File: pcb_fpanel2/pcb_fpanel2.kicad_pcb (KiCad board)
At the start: 2 copper layers, 11 parts, among them J1 Conn_01x09, SW1 SW_Push_LED, SW2 SW_Push_LED, SW3 SW_Push_LED, SW4 SW_Push_LED, SW5 SW_Push_LED

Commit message: Frontpanel pcb valmis
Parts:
- added D6: D, Diodes_THT:D_DO-35_SOD27_P7.62mm_Horizontal, F.Cu at (182.0, 117.0)
- added D7: D, Diodes_THT:D_DO-35_SOD27_P7.62mm_Horizontal, F.Cu at (178.0, 117.0)
- added D8: D, Diodes_THT:D_DO-35_SOD27_P7.62mm_Horizontal, F.Cu at (174.0, 117.0)
- added D9: D, Diodes_THT:D_DO-35_SOD27_P7.62mm_Horizontal, F.Cu at (170.0, 117.0)
- added REF**: MountingHole_4.3mm_M4, Mounting_Holes:MountingHole_4.3mm_M4, F.Cu at (140.0, 155.0)
- added REF**: MountingHole_4.3mm_M4, Mounting_Holes:MountingHole_4.3mm_M4, F.Cu at (60.0, 135.0)
- added REF**: MountingHole_4.3mm_M4, Mounting_Holes:MountingHole_4.3mm_M4, F.Cu at (140.0, 110.0)
- added SW6: SW_Push_LED, MX_Alps_Hybrid:MX-1U, F.Cu at (155.4, 138.4)
- added SW7: SW_Push_LED, MX_Alps_Hybrid:MX-1U, F.Cu at (155.4, 157.5)
- added SW8: SW_Push_LED, MX_Alps_Hybrid:MX-1U, F.Cu at (174.5, 157.5)
- added SW9: SW_Push_LED, MX_Alps_Hybrid:MX-1U, F.Cu at (174.4, 138.4)
- J1: value Conn_01x09 -> Conn_01x10; footprint Pin_Headers:Pin_Header_Straight_1x09_Pitch2.54mm -> Pin_Headers:Pin_Header_Straight_1x10_Pitch2.54mm; moved to B.Cu
- moved J1 116.4 mm to (142.0, 146.0)
- moved D3 84.6 mm to (129.0, 116.2)
- moved D4 84.6 mm to (129.0, 120.0)
- moved D5 84.6 mm to (129.0, 123.8)
- moved D2 83.7 mm to (113.0, 127.0)
- moved D1 81.4 mm to (113.0, 131.0)
- moved SW5 81.0 mm to (63.4, 112.0)
- moved SW3 80.9 mm to (101.5, 112.0)
- moved SW4 80.9 mm to (82.5, 112.0)
- moved SW1 69.2 mm to (126.3, 138.4)
- moved SW2 68.9 mm to (38.5, 138.4)
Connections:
- net Net-(D1-Pad1) renamed row_1
- J1 pad 1: Net-(J1-Pad1) -> led_1
- J1 pad 2: Net-(J1-Pad2) -> led_2
- J1 pad 3: Net-(J1-Pad3) -> GNDD
- J1 pad 4: Net-(J1-Pad4) -> column_1
- J1 pad 5: Net-(J1-Pad5) -> column_2
- J1 pad 7: Net-(J1-Pad7) -> column_3
- J1 pad 8: Net-(J1-Pad8) -> column_4
- J1 pad 9: Net-(J1-Pad9) -> column_5
- SW1 pad 2: Net-(J1-Pad5) -> column_1
- SW1 pad 3: Net-(J1-Pad7) -> led_2
- SW1 pad 4: Net-(J1-Pad8) -> GNDD
- SW2 pad 2: Net-(J1-Pad4) -> column_2
- SW2 pad 3: Net-(J1-Pad9) -> led_1
- SW2 pad 4: Net-(J1-Pad8) -> GNDD
- SW3 pad 2: Net-(J1-Pad3) -> column_3
- SW4 pad 2: Net-(J1-Pad2) -> column_4
- SW5 pad 2: Net-(J1-Pad1) -> column_5
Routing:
- net column_2: track 0.00 -> 158.4 mm
- net Net-(J1-Pad4): track 154.2 -> 0.00 mm
- net Net-(J1-Pad9): track 145.2 -> 0.00 mm
- net Net-(J1-Pad8): track 144.5 -> 0.00 mm
- net led_1: track 0.00 -> 119.7 mm
- net Net-(J1-Pad1): track 116.1 -> 0.00 mm
- net column_4: track 0.00 -> 112.8 mm
- net Net-(D6-Pad2): track 0.00 -> 104.4 mm
- net column_3: track 0.00 -> 104.1 mm
- net Net-(J1-Pad2): track 95.3 -> 0.00 mm
- net column_5: track 0.00 -> 92.1 mm
- net Net-(D7-Pad2): track 0.00 -> 85.0 mm
- net Net-(J1-Pad5): track 76.2 -> 0.00 mm
- net Net-(J1-Pad3): track 75.5 -> 0.00 mm
- net Net-(J1-Pad7): track 62.1 -> 0.00 mm
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- added copper zone on B.Cu, net GNDD
- removed copper zone on F.Cu, net (none)
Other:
- board outline added: 155 x 65 mm
- net class Default: clearance 0.2 -> 0.4; trace_width 0.25 -> 0.4
- rule trace_clearance: 0.2 -> 0.4

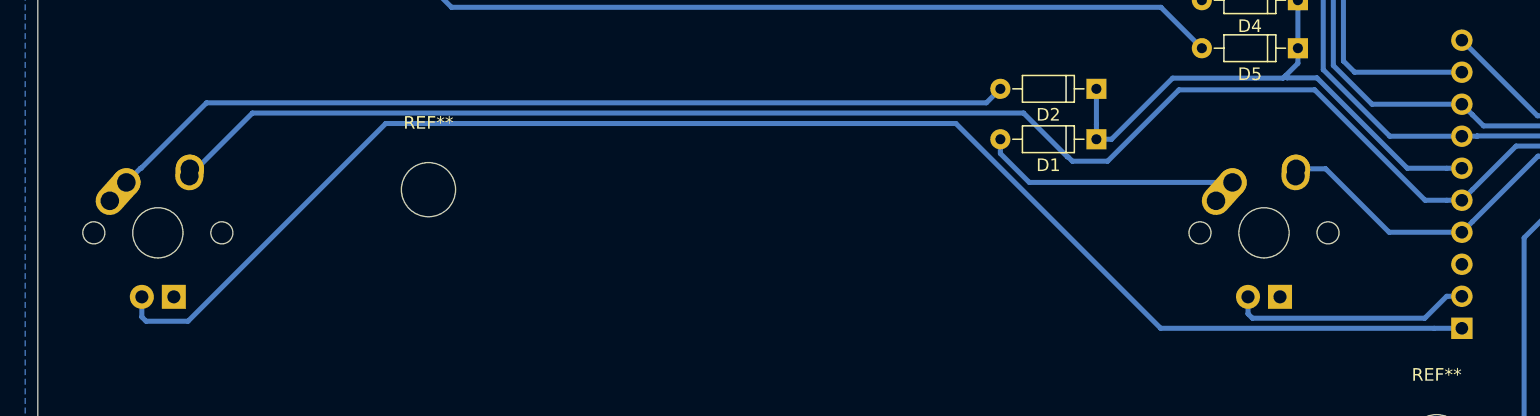
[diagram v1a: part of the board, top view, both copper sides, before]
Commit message: Frontpanel pcb korjaus: led-napit käännetty ja yhteensopivuus arduino pro micron kanssa
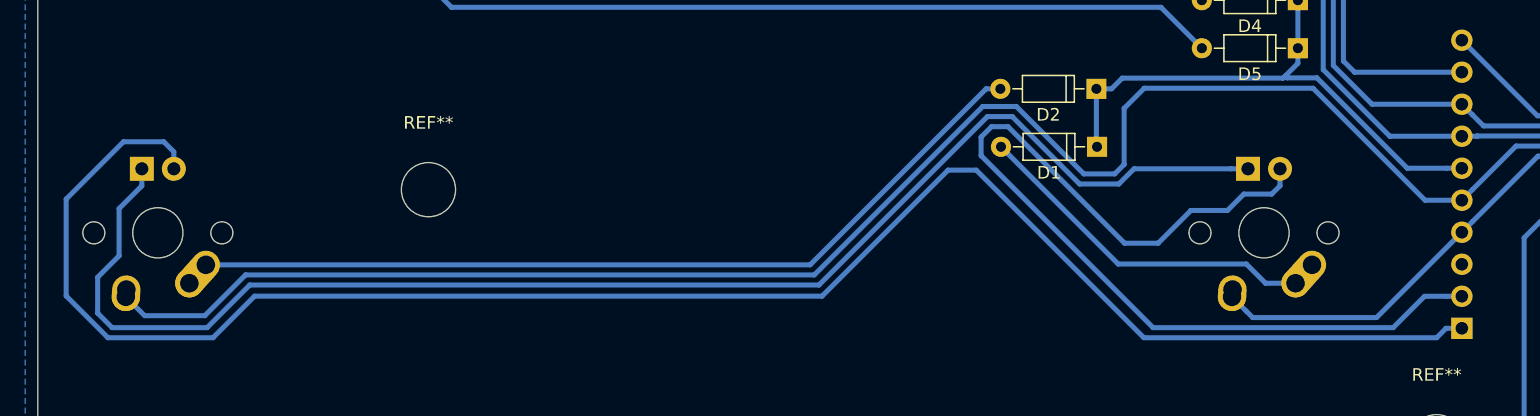
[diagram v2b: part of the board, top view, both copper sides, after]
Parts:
- moved D1 0.60 mm to (113.0, 131.6)
- turned SW1 to 180 degrees
- turned SW2 to 180 degrees
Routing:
- net GNDD: track 0.00 -> 114.3 mm
- net led_2: track 19.2 -> 77.4 mm
- net led_1: track 119.7 -> 143.2 mm
- net column_2: track 158.4 -> 172.6 mm
- net Net-(D1-Pad2): track 20.5 -> 27.9 mm
- net column_1: track 34.3 -> 40.8 mm
- net Net-(D2-Pad2): track 72.4 -> 68.8 mm
- net row_1: track 48.3 -> 47.3 mm

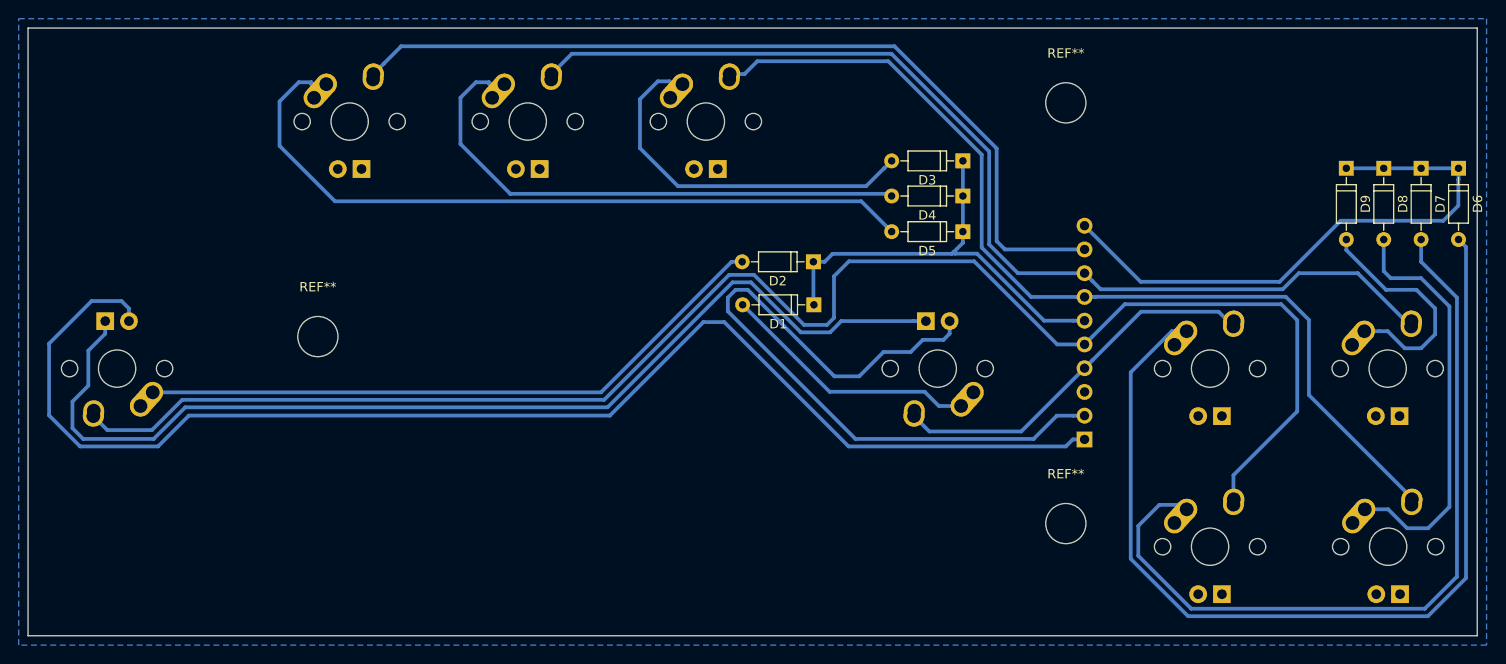
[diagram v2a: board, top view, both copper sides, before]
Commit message: fpanel1 ja fpanel2 välisen liittimen pin-järjestys korjattu vastaamaan toisiaan
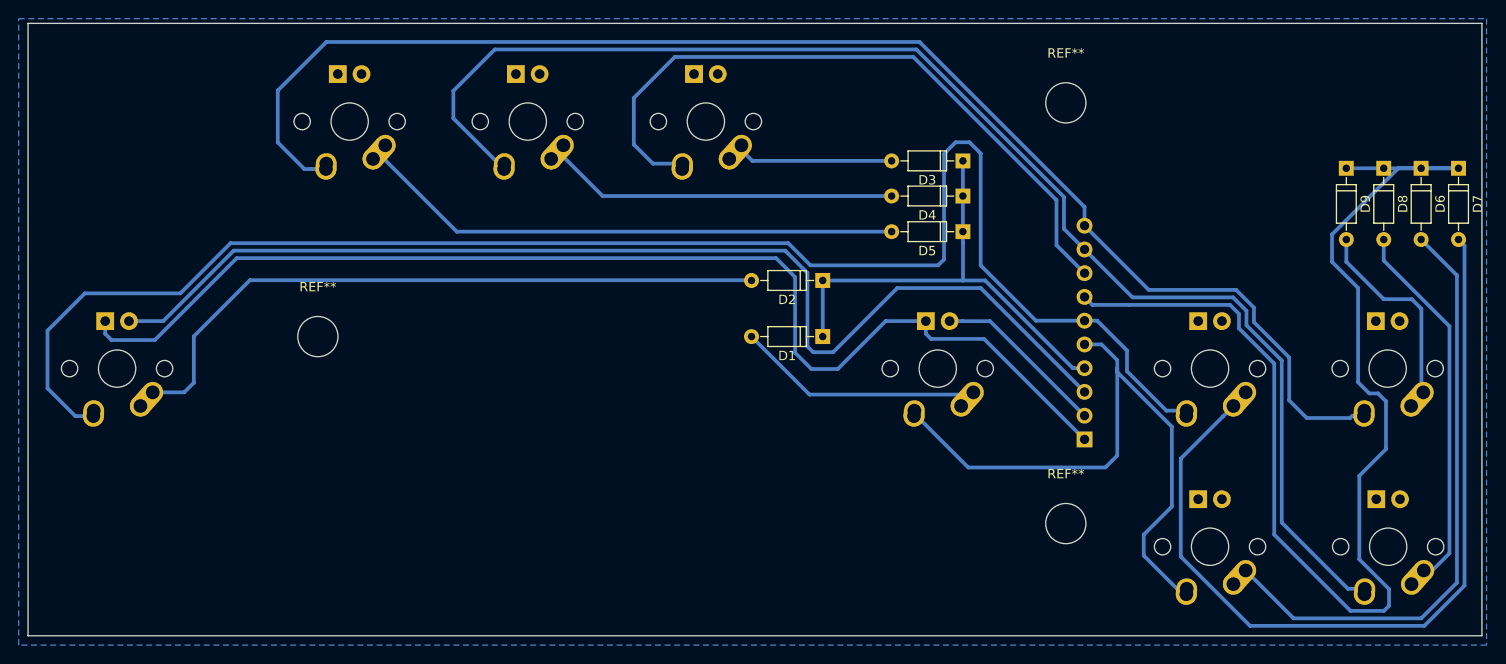
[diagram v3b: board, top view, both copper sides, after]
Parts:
- moved SW6 19.0 mm to (155.4, 157.5), turned to 180 degrees
- moved SW7 19.0 mm to (155.4, 138.4), turned to 180 degrees
- moved D6 4.00 mm to (178.0, 117.0)
- moved D7 4.00 mm to (182.0, 117.0)
- moved D1 3.53 mm to (114.0, 135.0)
- moved D2 2.24 mm to (114.0, 129.0)
- turned SW3 to 180 degrees
- turned SW4 to 180 degrees
- turned SW5 to 180 degrees
- turned SW8 to 180 degrees
- turned SW9 to 180 degrees
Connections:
- J1 pad 1: led_1 -> GNDD
- J1 pad 10: row_2 -> column_4
- J1 pad 3: GNDD -> led_1
- J1 pad 4: column_1 -> row_1
- J1 pad 5: column_2 -> column_1
- J1 pad 6: row_1 -> column_2
- J1 pad 7: column_3 -> row_2
- J1 pad 8: column_4 -> column_5
- J1 pad 9: column_5 -> column_3
- SW3 pad 2: column_3 -> column_5
- SW4 pad 2: column_4 -> column_3
- SW5 pad 2: column_5 -> column_4
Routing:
- net row_2: track 61.8 -> 131.9 mm
- net led_2: track 77.4 -> 18.6 mm
- net column_3: track 104.1 -> 146.9 mm
- net Net-(D6-Pad2): track 104.4 -> 64.6 mm
- net column_4: track 112.8 -> 151.7 mm
- net column_1: track 40.8 -> 69.1 mm
- net Net-(D3-Pad2): track 40.4 -> 17.0 mm
- net led_1: track 143.2 -> 121.9 mm
- net Net-(D5-Pad2): track 80.1 -> 58.9 mm
- net Net-(D4-Pad2): track 58.9 -> 38.1 mm
- net column_5: track 92.1 -> 73.5 mm
- net GNDD: track 114.3 -> 127.8 mm
- net Net-(D7-Pad2): track 85.0 -> 90.9 mm
- net Net-(D8-Pad2): track 44.3 -> 40.0 mm
- net row_1: track 47.3 -> 50.7 mm
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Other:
- board size 155 x 65 mm -> 155.5 x 65.5 mm

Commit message: Näppäinmatriisin srakkeille lisätty etuvastukset
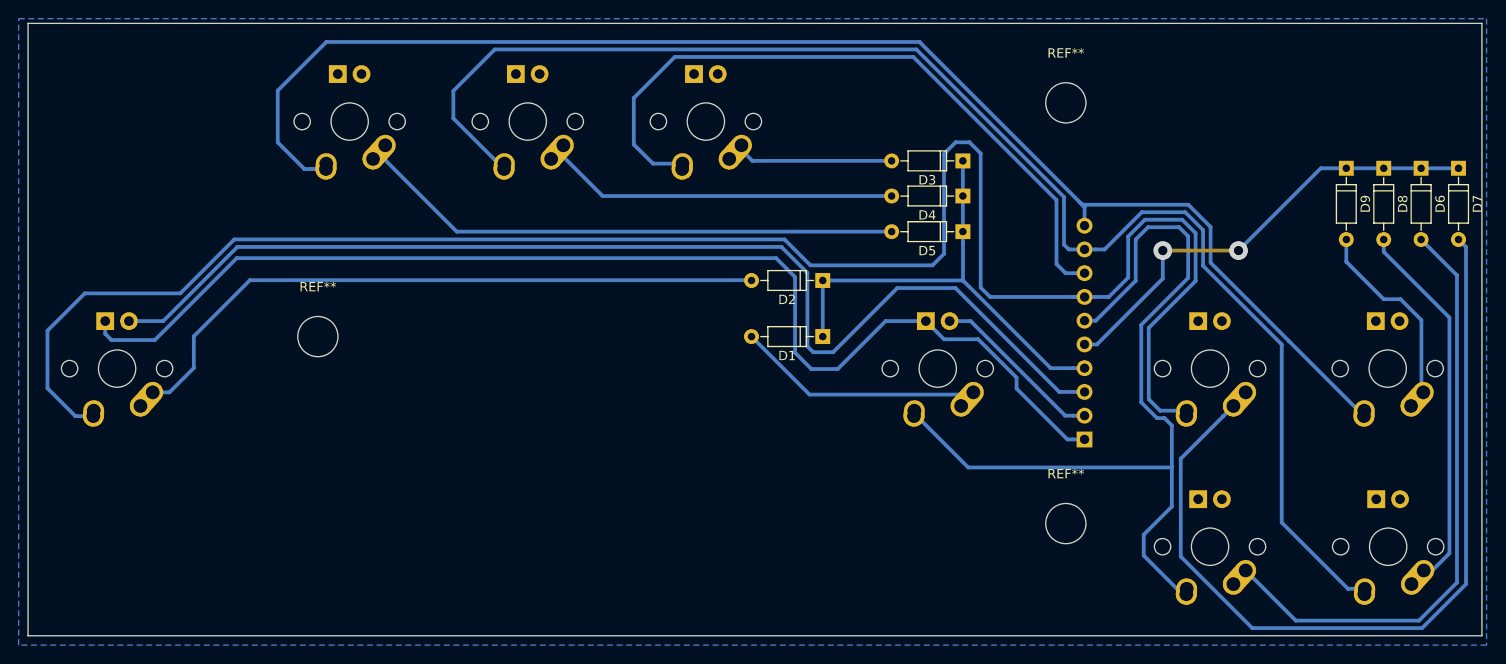
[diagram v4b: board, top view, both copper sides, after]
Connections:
- J1 pad 5: column_1 -> row_2
- J1 pad 6: column_2 -> column_1
- J1 pad 7: row_2 -> column_2
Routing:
- net row_2: track 131.9 -> 49.6 mm, vias 0 -> 2
- net column_2: track 171.6 -> 198.5 mm
- net column_1: track 69.1 -> 93.8 mm
- net column_3: track 146.9 -> 153.5 mm
- net column_5: track 73.5 -> 74.6 mm
- net Net-(D2-Pad2): track 71.9 -> 71.0 mm
- net Net-(D9-Pad2): track 21.5 -> 20.8 mm
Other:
- net class Default: via_dia 0.8 -> 2; via_drill 0.4 -> 1

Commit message: Reikien siirtelyä
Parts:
- moved REF** 33.8 mm to (108.0, 144.0)
- moved REF** 30.5 mm to (34.0, 119.0)
- moved REF** 19.4 mm to (159.4, 109.0)
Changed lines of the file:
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@@
   (general
     (thickness 1.6)
-    (drawings 6)
+    (drawings 10)
     (tracks 193)
     (zones 0)
@@
     (visible_elements 7FFFFFFF)
     (pcbplotparams
-      (layerselection 0x010fc_ffffffff)
+      (layerselection 0x00000_fffffffe)
       (usegerberextensions false)
       (usegerberattributes false)
@@
       (excludeedgelayer true)
       (linewidth 0.100000)
-      (plotframeref false)
+      (plotframeref true)
       (viasonmask false)
       (mode 1)
@@
       (psnegative false)
       (psa4output false)
-      (plotreference true)
-      (plotvalue true)
+      (plotreference false)
+      (plotvalue false)
       (plotinvisibletext false)
-      (padsonsilk false)
+      (padsonsilk true)
       (subtractmaskfromsilk false)
-      (outputformat 1)
+      (outputformat 5)
       (mirror false)
       (drillshape 1)
       (scaleselection 1)
-      (outputdirectory ""))
+      (outputdirectory "./"))
   )
   (net 0 "")
@@
   )
   (module Mounting_Holes:MountingHole_4.3mm_M4 (layer F.Cu)
-    (at 140 155)
+    (at 108 144)
     (descr "Mounting Hole 4.3mm, no annular, M4")
     (tags "mounting hole 4.3mm no annular m4")
@@
   )
   (module Mounting_Holes:MountingHole_4.3mm_M4 (layer F.Cu)
-    (at 60 135)
+    (at 34 119)
     (descr "Mounting Hole 4.3mm, no annular, M4")
     (tags "mounting hole 4.3mm no annular m4")
@@
   )
   (module Mounting_Holes:MountingHole_4.3mm_M4 (layer F.Cu)
-    (at 140 110)
+    (at 159.4 109)
     (descr "Mounting Hole 4.3mm, no annular, M4")
     (tags "mounting hole 4.3mm no annular m4")
@@
       (net 23 column_4))
   )
+  (dimension 19.9 (width 0.12) (layer F.SilkS)
+    (gr_text "19.900 mm" (at 160.67 118.95 90) (layer F.SilkS)
+      (effects (font (size 1 1) (thickness 0.15)))
+    )
+    (feature1 (pts (xy 159.4 109) (xy 159.986421 109)))
+    (feature2 (pts (xy 159.4 128.9) (xy 159.986421 128.9)))
+    (crossbar (pts (xy 159.4 128.9) (xy 159.4 109)))
+    (arrow1a (pts (xy 159.4 109) (xy 159.986421 110.126504)))
+    (arrow1b (pts (xy 159.4 109) (xy 158.813579 110.126504)))
+    (arrow2a (pts (xy 159.4 128.9) (xy 159.986421 127.773496)))
+    (arrow2b (pts (xy 159.4 128.9) (xy 158.813579 127.773496)))
+  )
+  (dimension 13.5 (width 0.12) (layer F.SilkS)
+    (gr_text "13.500 mm" (at 152.65 108.13) (layer F.SilkS)
+      (effects (font (size 1 1) (thickness 0.15)))
+    )
+    (feature1 (pts (xy 159.4 128.9) (xy 159.4 108.813579)))
+    (feature2 (pts (xy 145.9 128.9) (xy 145.9 108.813579)))
+    (crossbar (pts (xy 145.9 109.4) (xy 159.4 109.4)))
+    (arrow1a (pts (xy 159.4 109.4) (xy 158.273496 109.986421)))
+    (arrow1b (pts (xy 159.4 109.4) (xy 158.273496 108.813579)))
+    (arrow2a (pts (xy 145.9 109.4) (xy 147.026504 109.986421)))
+    (arrow2b (pts (xy 145.9 109.4) (xy 147.026504 108.813579)))
+  )
+  (dimension 86 (width 0.12) (layer F.SilkS)
+    (gr_text "86.000 mm" (at 72 101.73) (layer F.SilkS)
+      (effects (font (size 1 1) (thickness 0.15)))
+    )
+    (feature1 (pts (xy 115 104) (xy 115 102.413579)))
+    (feature2 (pts (xy 29 104) (xy 29 102.413579)))
+    (crossbar (pts (xy 29 103) (xy 115 103)))
+    (arrow1a (pts (xy 115 103) (xy 113.873496 103.586421)))
+    (arrow1b (pts (xy 115 103) (xy 113.873496 102.413579)))
+    (arrow2a (pts (xy 29 103) (xy 30.126504 103.586421)))
+    (arrow2b (pts (xy 29 103) (xy 30.126504 102.413579)))
+  )
+  (dimension 80 (width 0.12) (layer F.SilkS)
+    (gr_text "80.000 mm" (at 69 151.27) (layer F.SilkS)
+      (effects (font (size 1 1) (thickness 0.15)))
+    )
+    (feature1 (pts (xy 109 150) (xy 109 150.586421)))
+    (feature2 (pts (xy 29 150) (xy 29 150.586421)))
+    (crossbar (pts (xy 29 150) (xy 109 150)))
+    (arrow1a (pts (xy 109 150) (xy 107.873496 150.586421)))
+    (arrow1b (pts (xy 109 150) (xy 107.873496 149.413579)))
+    (arrow2a (pts (xy 29 150) (xy 30.126504 150.586421)))
+    (arrow2b (pts (xy 29 150) (xy 30.126504 149.413579)))
+  )
   (dimension 65.5 (width 0.12) (layer F.SilkS)
